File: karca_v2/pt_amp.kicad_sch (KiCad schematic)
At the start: 19 parts, among them J6 Screw_Terminal_01x08, U10 TLV9304xD, U11 MCP3208, U12 NUP4202, U8 TPS7A24, U9 TLV9304xD

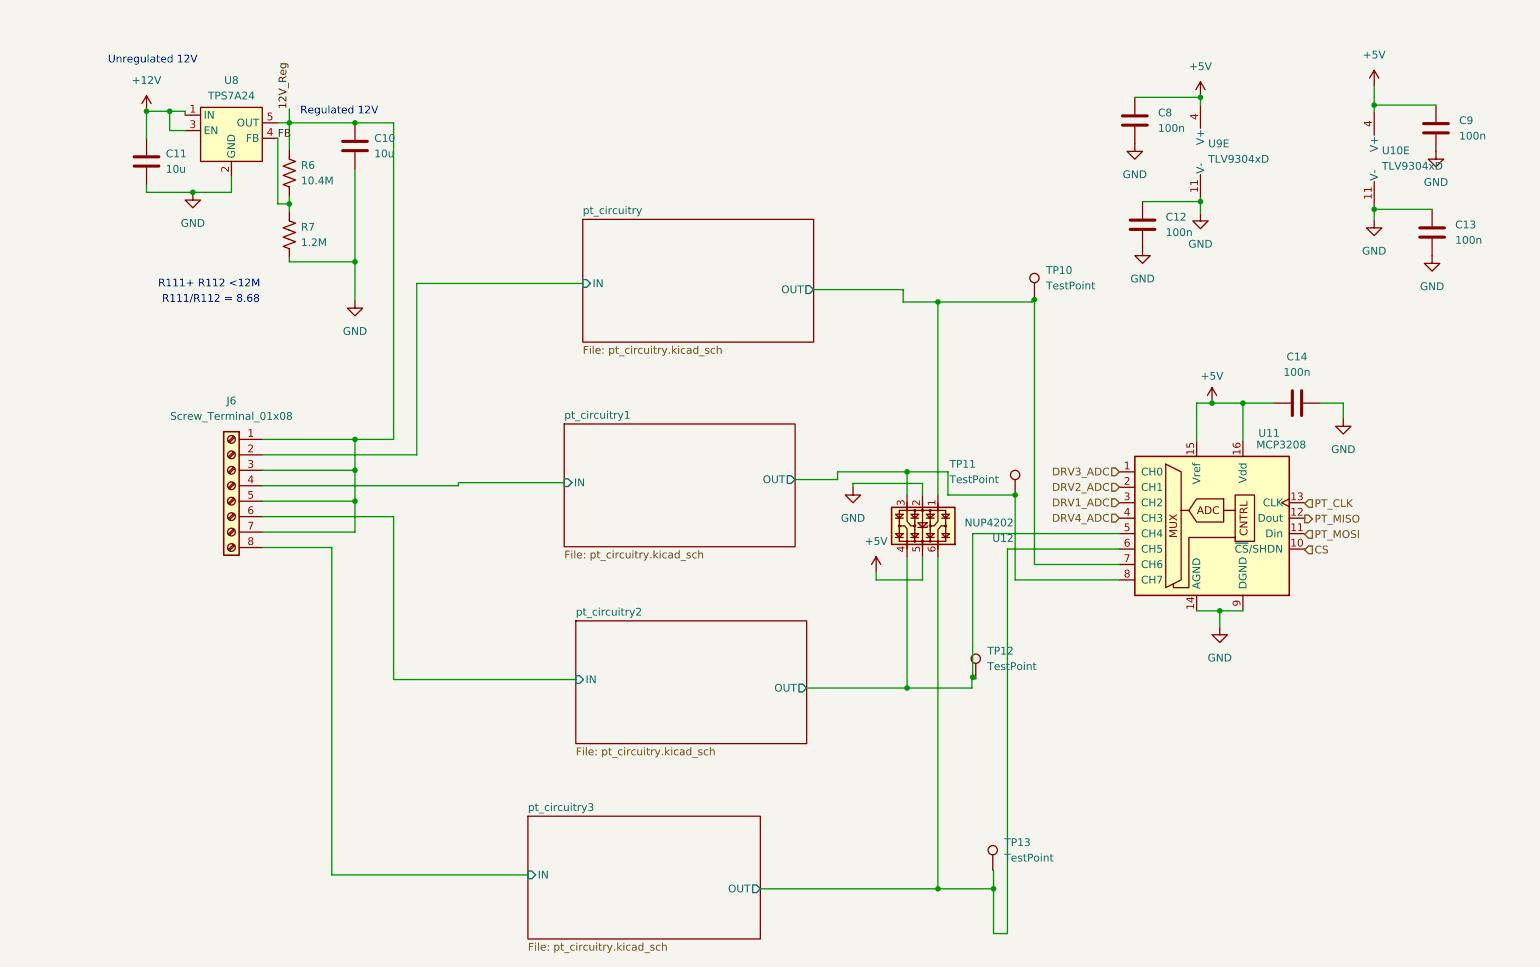
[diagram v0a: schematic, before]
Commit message: Fixed ground capacitors
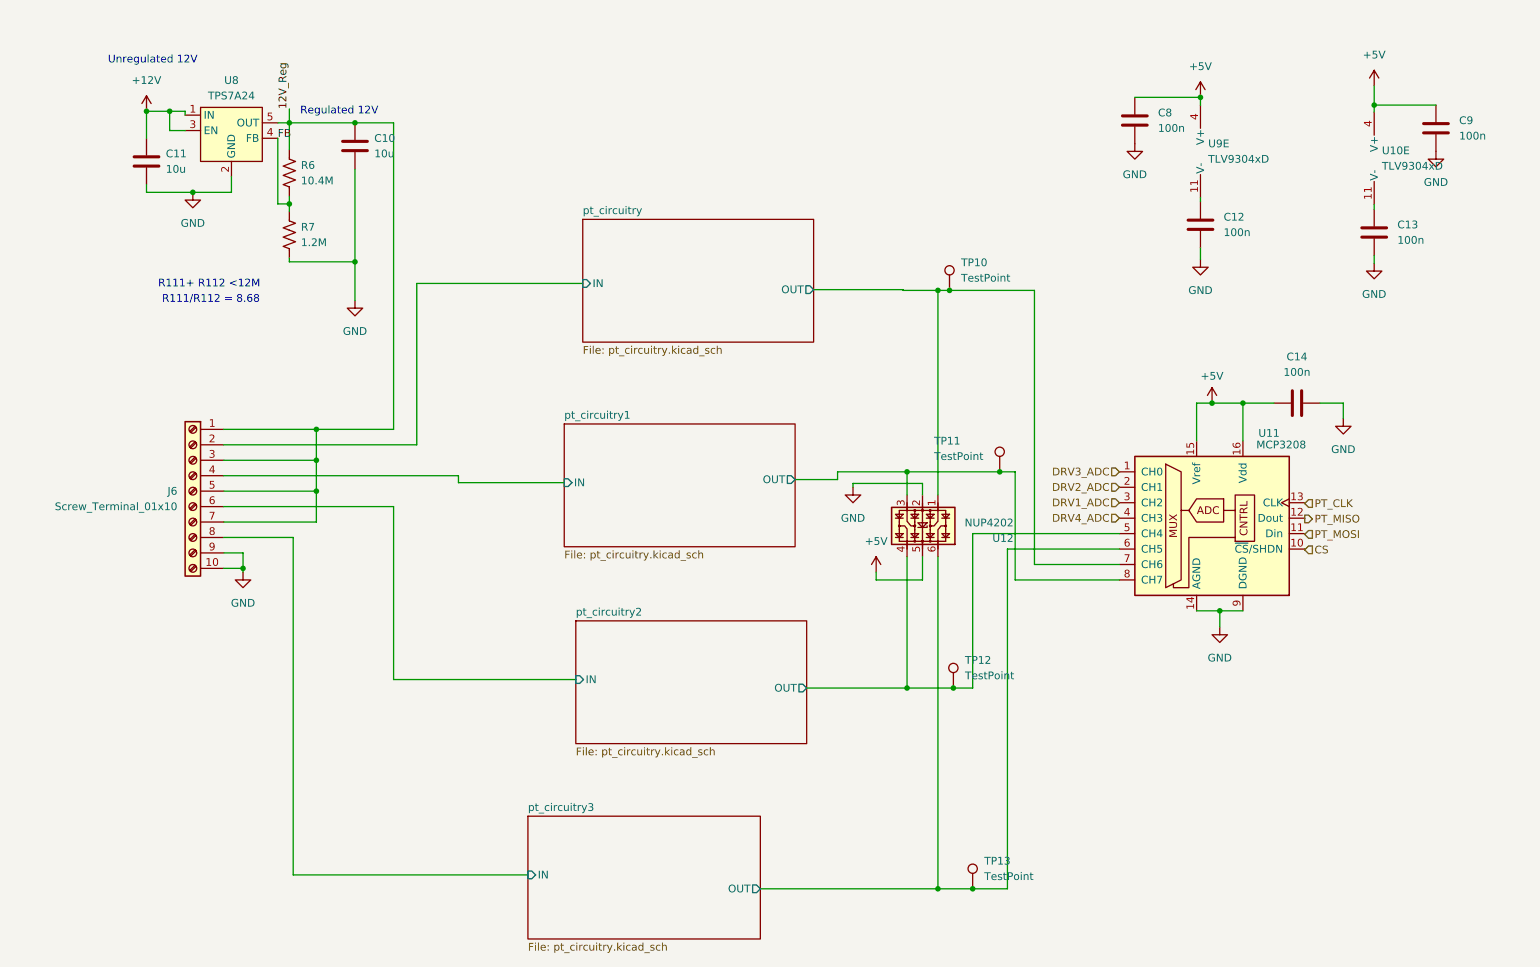
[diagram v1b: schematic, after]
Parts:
- removed J6: Screw_Terminal_01x08, terminal blocks:P-2604-1108, symbol Connector:Screw_Terminal_01x08
- added J6: Screw_Terminal_01x10, terminal blocks:P-2604-1110, symbol Connector:Screw_Terminal_01x10
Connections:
- net 12V_Reg: now also J6.1 (Pin_1), J6.3 (Pin_3), J6.5 (Pin_5), J6.7 (Pin_7)
- net GND: now also J6.10 (Pin_10), J6.9 (Pin_9); no longer C12.2, C13.2, U10.11 (V-), U9.11 (V-)
- net pt_circuitry/IN: now also J6.2 (Pin_2)
- net pt_circuitry1/IN: now also J6.4 (Pin_4)
- net pt_circuitry2/IN: now also J6.6 (Pin_6)
- net pt_circuitry3/IN: now also J6.8 (Pin_8)
- new net: C12.2, U9.11 (V-)
- new net: C13.2, U10.11 (V-)
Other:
- moved on the sheet: TP10, TP11, TP12, TP13

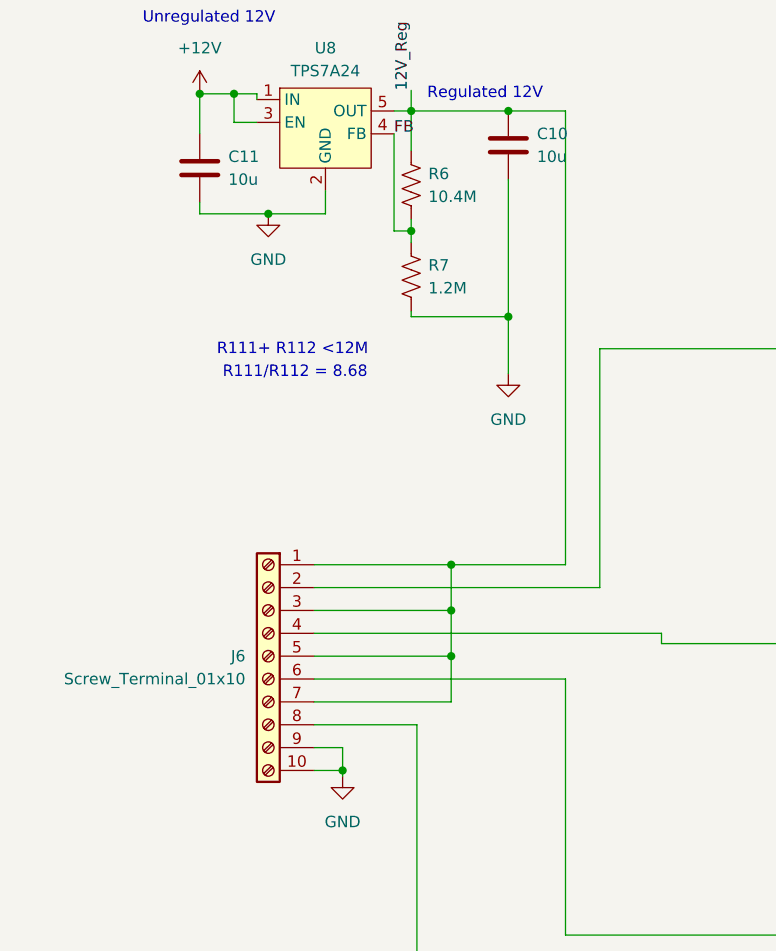
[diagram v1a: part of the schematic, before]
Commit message: cleaned up documentation. Added production files and BOM. Marked Thermocouple components and THT components as DNP (excluded them from BOM too) to match version sent to JLCPCB for fabrication
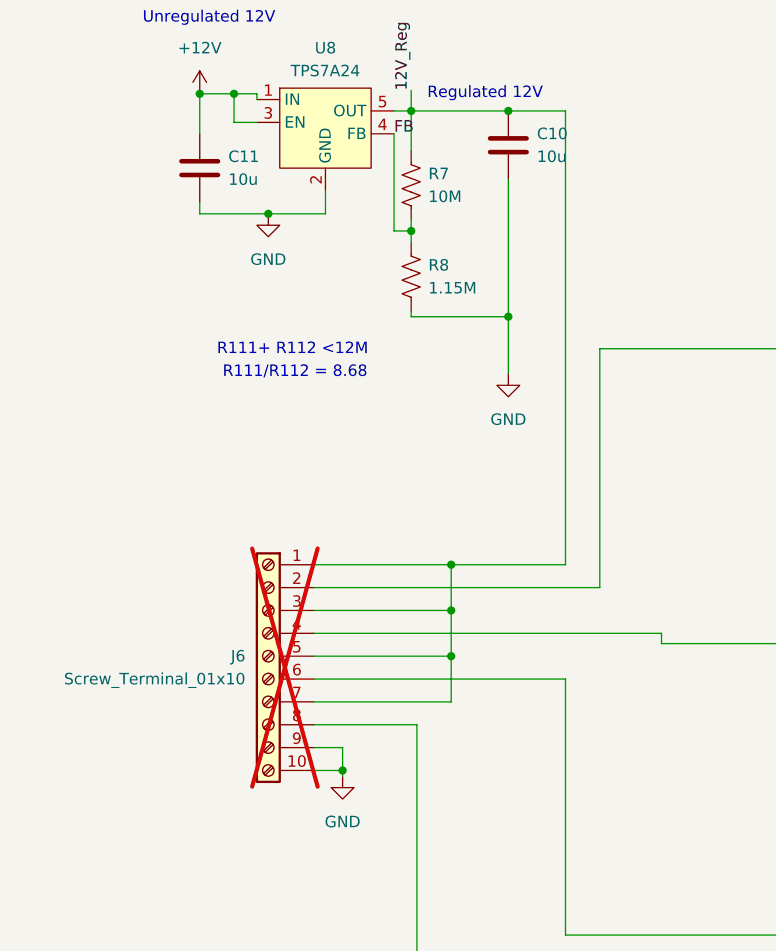
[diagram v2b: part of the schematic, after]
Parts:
- J6: now not fitted; now left out of the parts list
- R7: renamed from R6; value 10.4M -> 10M
- R8: renamed from R7; value 1.2M -> 1.15M
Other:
- company: (none) -> Rice Eclipse
- title: (none) -> kARCA 2.0 Engine Control System

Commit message: revisions for V2.1
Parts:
- removed C12, C13: 100n, Capacitor_SMD:C_1206_3216Metric, symbol Device:C
- J6: footprint terminal blocks:P-2604-1110 -> custom-footprints:P-2604-1110
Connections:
- net GND: now also U10.11 (V-), U9.11 (V-)
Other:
- note added: "Vout = Vfb(1+ R111/R112) Vfb = 1.24V"
- moved on the sheet: C10, C11, C14, C8, C9, J6, R7, R8, TP10, TP11, TP12, TP13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

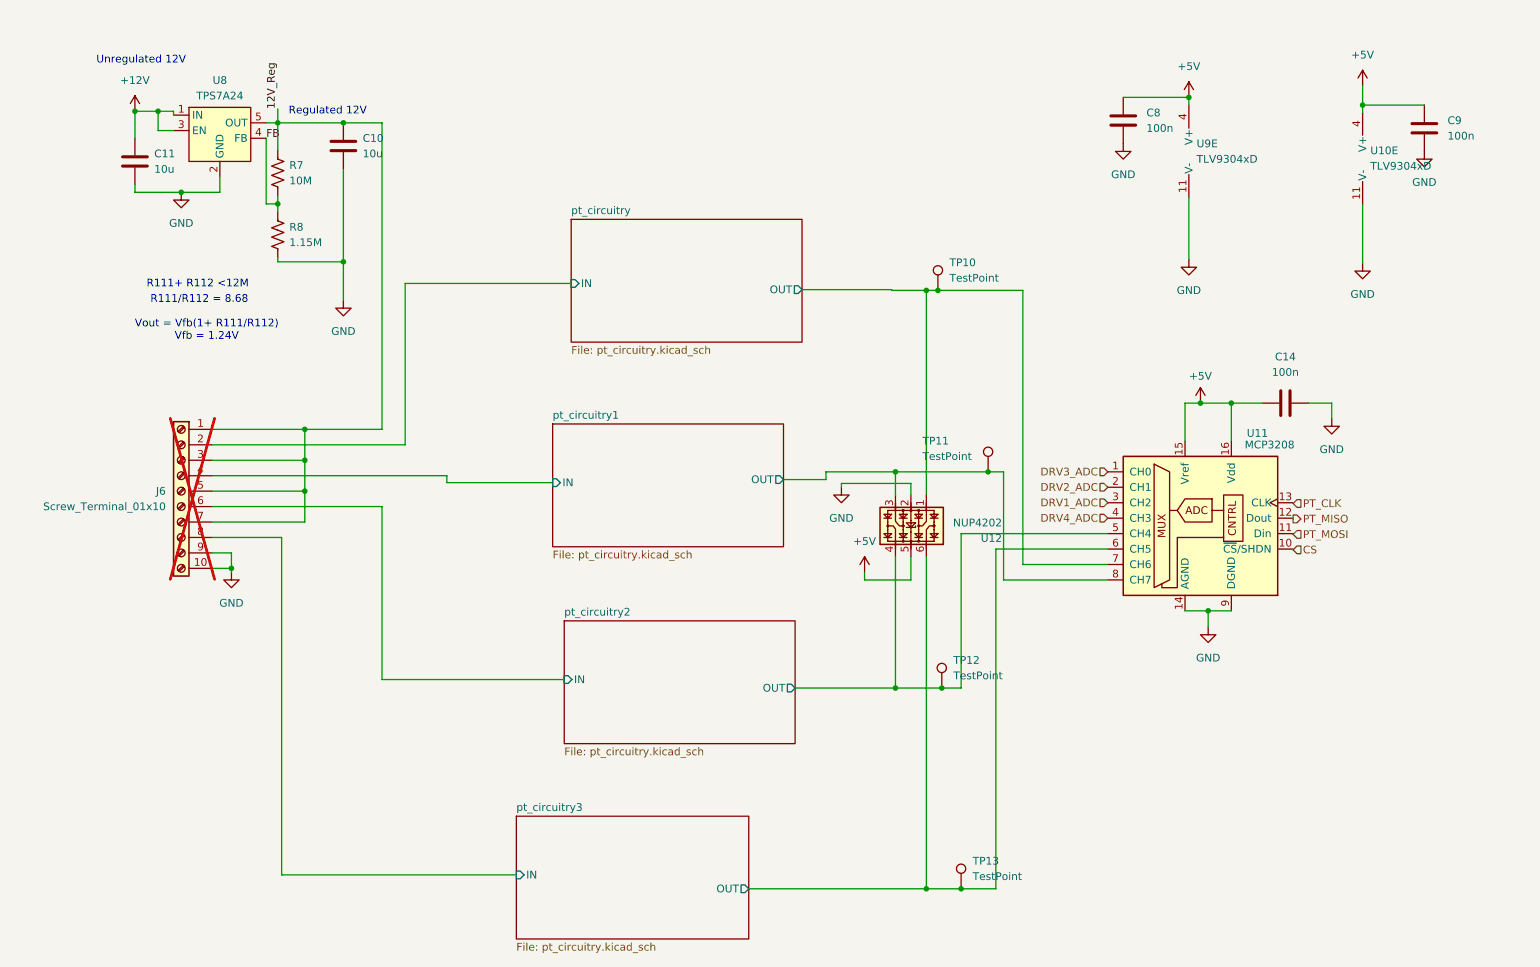
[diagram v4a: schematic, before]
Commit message: reorganized ADCs
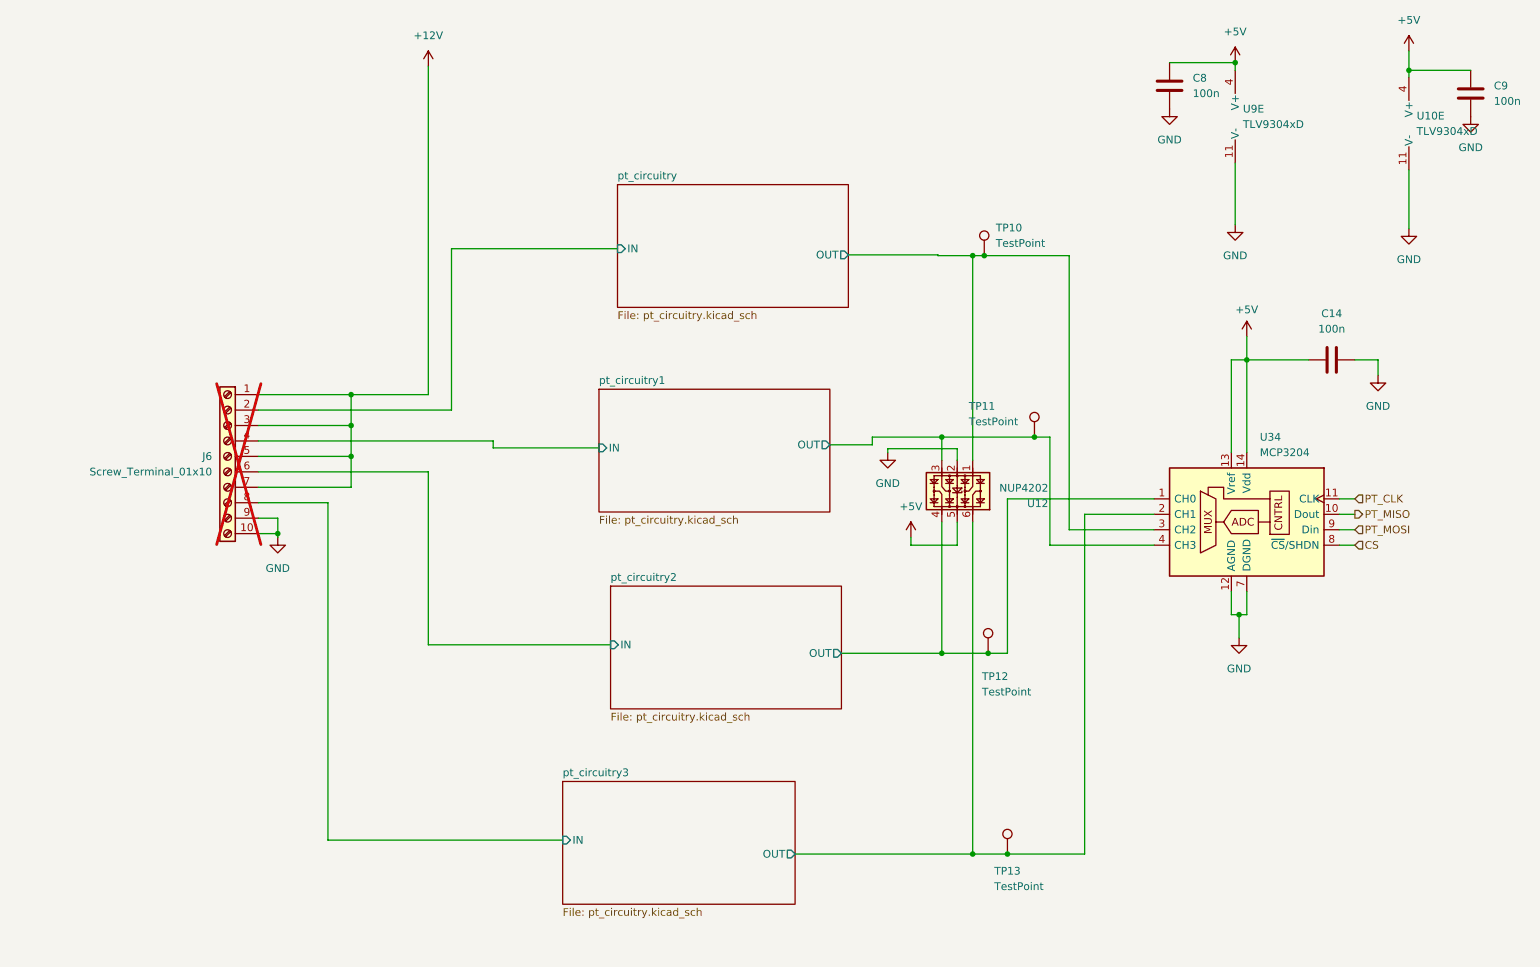
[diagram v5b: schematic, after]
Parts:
- removed C10, C11: 10u, Capacitor_SMD:C_1206_3216Metric, symbol Device:C
- removed R7: 10M, Resistor_SMD:R_1206_3216Metric, symbol Device:R_US
- removed R8: 1.15M, Resistor_SMD:R_1206_3216Metric, symbol Device:R_US
- removed U11: MCP3208, Package_SO:SOIC-16_3.9x9.9mm_P1.27mm, symbol Analog_ADC:MCP3208
- removed U8: TPS7A24, Package_TO_SOT_SMD:SOT-23-5, symbol karca_lib:TPS7A24
- added U34: MCP3204, symbol Analog_ADC:MCP3204
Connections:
- net 12V_Reg is gone; now on net +12V: J6.1 (Pin_1), J6.3 (Pin_3), J6.5 (Pin_5), J6.7 (Pin_7)
- net +5V: now also U34.13 (Vref), U34.14 (Vdd)
- net CS: now also U34.8 (~{CS}/SHDN)
- net GND: now also U34.12 (AGND), U34.7 (DGND)
- net PT_CLK: now also U34.11 (CLK)
- net PT_MISO: now also U34.10 (Dout)
- net PT_MOSI: now also U34.9 (Din)
- net pt_circuitry/OUT: now also U34.3 (CH2)
- net pt_circuitry1/OUT: now also U34.4 (CH3)
- net pt_circuitry2/OUT: now also U34.1 (CH0)
- net pt_circuitry3/OUT: now also U34.2 (CH1)
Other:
- note removed: "R111+ R112 <12M"
- note removed: "R111/R112 = 8.68"
- note removed: "Regulated 12V"
- note removed: "Unregulated 12V"
- note removed: "Vout = Vfb(1+ R111/R112) Vfb = 1.24V"
- moved on the sheet: C14, C8, C9, J6, TP10, TP11, TP12, TP13, U10E, U12, U9E
